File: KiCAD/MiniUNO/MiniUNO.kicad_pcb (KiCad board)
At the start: 2 copper layers, 22 x 18 mm, 19 parts, among them J1 USB_B_Micro, J2 Conn_01x11, J3 Conn_01x11, J4 Conn_01x07, U1 ATmega32U4-A, Y1 830108288709

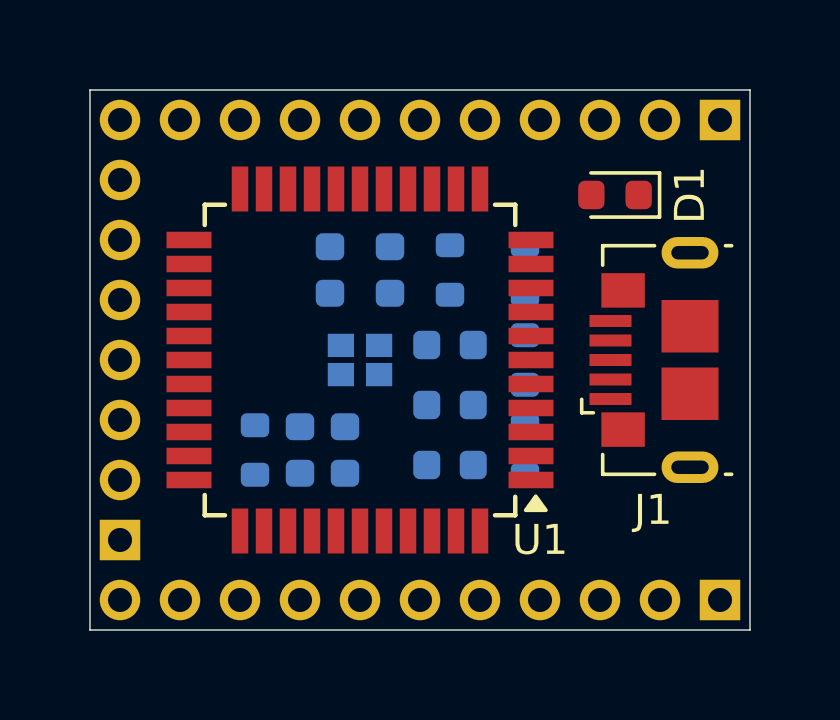
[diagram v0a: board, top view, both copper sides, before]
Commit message: Added a user controlled LED
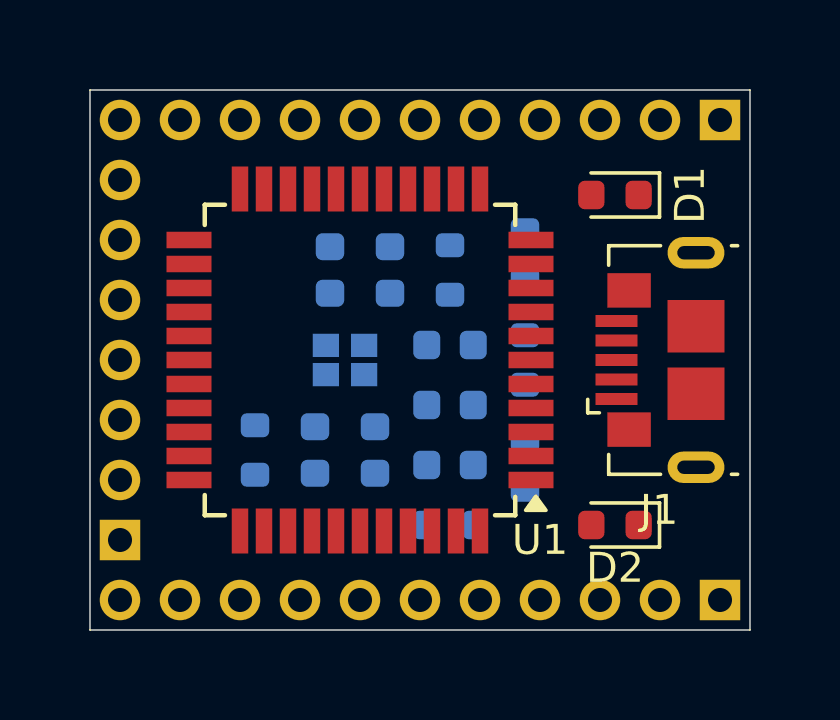
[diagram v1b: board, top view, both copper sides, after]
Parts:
- added D2: LED, LED_SMD:LED_0603_1608Metric, F.Cu at (8.50, 5.50)
- added R6: 330, Resistor_SMD:R_0603_1608Metric, B.Cu at (3.00, 5.50)
- moved C3 1.00 mm to (0.50, 3.00)
- moved C4 0.50 mm to (-1.50, 3.00)
- moved R2 0.50 mm to (5.50, 3.50)
- moved R5 0.50 mm to (5.50, -3.50)
- moved Y1 0.50 mm to (-0.50, 0.00)
- moved J1 0.20 mm to (10.0, 0.00)
- turned R3 to 90 degrees
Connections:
- C3 pad 1: VCC -> RESET
- C4 pad 1: VCC -> RESET
- C5 pad 1: VCC -> RESET
- J1 pad 1: VCC -> RESET
- J2 pad 1: unconnected-(J2-Pin_1-Pad1) -> RESET
- J2 pad 2: unconnected-(J2-Pin_2-Pad2) -> RESET
- J3 pad 1: unconnected-(J3-Pin_1-Pad1) -> GND
- R4 pad 2: VCC -> RESET
- R5 pad 1: VCC -> RESET
- U1 pad 1: unconnected-(U1-PE6-Pad1) -> USER_LED
- U1 pad 14: VCC -> RESET
- U1 pad 2: VCC -> RESET
- U1 pad 24: VCC -> RESET
- U1 pad 34: VCC -> RESET
- U1 pad 44: VCC -> RESET
- U1 pad 7: VCC -> RESET

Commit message: Minor changes
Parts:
- Y1: footprint Crystal:830108288709 -> Crystal:830108288709_Handsolderable
- moved R6 4.30 mm to (6.50, 3.00)
- moved R2 2.69 mm to (6.50, 1.00), turned to 180 degrees
- moved R1 1.41 mm to (6.50, -1.00), turned to 180 degrees
- moved R5 1.12 mm to (6.50, -3.00), turned to 0 degrees
- moved C1 0.50 mm to (-1.50, -3.00), turned to 90 degrees
- moved C2 0.50 mm to (0.50, -3.00)
- moved R4 0.50 mm to (2.50, -3.00)
- turned C7 to 180 degrees
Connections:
- C3 pad 1: RESET -> VCC
- C4 pad 1: RESET -> VCC
- C5 pad 1: RESET -> VCC
- C7 pad 1: Net-(U1-AREF) -> AREF
- J1 pad 1: RESET -> VCC
- J2 pad 1: RESET -> VCC
- J2 pad 10: unconnected-(J2-Pin_10-Pad10) -> D2/SDA
- J2 pad 11: unconnected-(J2-Pin_11-Pad11) -> D3/SCL
- J2 pad 3: unconnected-(J2-Pin_3-Pad3) -> SS
- J2 pad 4: unconnected-(J2-Pin_4-Pad4) -> SCK
- J2 pad 5: unconnected-(J2-Pin_5-Pad5) -> MOSI
- J2 pad 6: unconnected-(J2-Pin_6-Pad6) -> MISO
- J2 pad 7: unconnected-(J2-Pin_7-Pad7) -> CTS
- J2 pad 8: unconnected-(J2-Pin_8-Pad8) -> D0/RX
- J2 pad 9: unconnected-(J2-Pin_9-Pad9) -> D1/TX
- J3 pad 10: unconnected-(J3-Pin_10-Pad10) -> D12
- J3 pad 11: unconnected-(J3-Pin_11-Pad11) -> D11
- J3 pad 2: unconnected-(J3-Pin_2-Pad2) -> AREF
- J3 pad 3: unconnected-(J3-Pin_3-Pad3) -> A5
- J3 pad 4: unconnected-(J3-Pin_4-Pad4) -> A4
- J3 pad 5: unconnected-(J3-Pin_5-Pad5) -> A3
- J3 pad 6: unconnected-(J3-Pin_6-Pad6) -> A2
- J3 pad 7: unconnected-(J3-Pin_7-Pad7) -> A1
- J3 pad 8: unconnected-(J3-Pin_8-Pad8) -> A0
- J3 pad 9: unconnected-(J3-Pin_9-Pad9) -> D13/USER_LED
- J4 pad 1: unconnected-(J4-Pin_1-Pad1) -> D4
- J4 pad 2: unconnected-(J4-Pin_2-Pad2) -> D5
- J4 pad 3: unconnected-(J4-Pin_3-Pad3) -> D6
- J4 pad 4: unconnected-(J4-Pin_4-Pad4) -> D7
- J4 pad 5: unconnected-(J4-Pin_5-Pad5) -> D8
- J4 pad 6: unconnected-(J4-Pin_6-Pad6) -> D9
- J4 pad 7: unconnected-(J4-Pin_7-Pad7) -> D10
- R4 pad 1: Net-(U1-~{RESET}) -> RESET
- R4 pad 2: RESET -> VCC
- R5 pad 1: RESET -> VCC
- R6 pad 1: USER_LED -> D13/USER_LED
- U1 pad 1: USER_LED -> D7
- U1 pad 10: unconnected-(U1-PB2-Pad10) -> MOSI
- U1 pad 11: unconnected-(U1-PB3-Pad11) -> MISO
- U1 pad 12: unconnected-(U1-PB7-Pad12) -> D11
- U1 pad 13: Net-(U1-~{RESET}) -> RESET
- U1 pad 14: RESET -> VCC
- U1 pad 18: unconnected-(U1-PD0-Pad18) -> D3/SCL
- U1 pad 19: unconnected-(U1-PD1-Pad19) -> D2/SDA
- U1 pad 2: RESET -> VCC
- U1 pad 20: unconnected-(U1-PD2-Pad20) -> D0/RX
- U1 pad 21: unconnected-(U1-PD3-Pad21) -> D1/TX
- U1 pad 22: unconnected-(U1-PD5-Pad22) -> CTS
- U1 pad 24: RESET -> VCC
- U1 pad 25: unconnected-(U1-PD4-Pad25) -> D4
- U1 pad 26: unconnected-(U1-PD6-Pad26) -> D12
- U1 pad 27: unconnected-(U1-PD7-Pad27) -> D6
- U1 pad 28: unconnected-(U1-PB4-Pad28) -> D8
- U1 pad 29: unconnected-(U1-PB5-Pad29) -> D9
- U1 pad 30: unconnected-(U1-PB6-Pad30) -> D10
- U1 pad 31: unconnected-(U1-PC6-Pad31) -> D5
- U1 pad 32: unconnected-(U1-PC7-Pad32) -> D13/USER_LED
- U1 pad 34: RESET -> VCC
- U1 pad 36: unconnected-(U1-PF7-Pad36) -> A0
- U1 pad 37: unconnected-(U1-PF6-Pad37) -> A1
- U1 pad 38: unconnected-(U1-PF5-Pad38) -> A2
- U1 pad 39: unconnected-(U1-PF4-Pad39) -> A3
- U1 pad 40: unconnected-(U1-PF1-Pad40) -> A4
- U1 pad 41: unconnected-(U1-PF0-Pad41) -> A5
- U1 pad 42: Net-(U1-AREF) -> AREF
- U1 pad 44: RESET -> VCC
- U1 pad 7: RESET -> VCC
- U1 pad 8: unconnected-(U1-PB0-Pad8) -> SS
- U1 pad 9: unconnected-(U1-PB1-Pad9) -> SCK

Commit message: Lots more work
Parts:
- added C8: 1uF, Capacitor_SMD:C_0603_1608Metric, B.Cu at (11.8, -5.50)
- added C9: 1uF, Capacitor_SMD:C_0603_1608Metric, B.Cu at (11.8, 5.50)
- added IC1: AZ1117CR2-5.0TRG1, AZ1117CR2-5.0TRG1:AP738133Y13, B.Cu at (8.64, 0.00)
- added Q1: FDN340P, Package_TO_SOT_SMD:SuperSOT-3, B.Cu at (8.50, 4.75)
- added Q2: PMV48XP, Package_TO_SOT_SMD:SOT-23, B.Cu at (8.56, -4.75)
- moved J4 12.0 mm to (-8.00, -6.00), turned to 180 degrees
- moved C3 8.14 mm to (-5.00, -3.00)
- moved C5 1.58 mm to (1.50, 3.00)
- moved C6 1.58 mm to (1.50, -1.00)
- moved C7 1.58 mm to (1.50, 1.00)
- moved C1 1.50 mm to (-3.00, -3.00)
- moved C2 1.50 mm to (-1.00, -3.00)
- moved R1 1.50 mm to (5.00, -1.00)
- moved R2 1.50 mm to (5.00, 1.00)
- moved R5 1.50 mm to (5.00, -3.00)
- moved R6 1.50 mm to (5.00, 3.00)
- moved Y1 1.50 mm to (-2.00, 0.00)
- moved R4 1.00 mm to (1.50, -3.00), turned to 0 degrees
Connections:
- net Net-(U1-D+) renamed D+
- net Net-(U1-D-) renamed D-
- net Net-(U1-UCAP) renamed UCAP
- C3 pad 1: VCC -> +5V
- C4 pad 1: VCC -> +5V
- C5 pad 1: VCC -> +5V
- J1 pad 1: VCC -> VUSB
- J2 pad 1: VCC -> +5V
- J3 pad 2: AREF -> VIN
- R4 pad 2: VCC -> +5V
- R5 pad 1: VCC -> +5V
- U1 pad 14: VCC -> +5V
- U1 pad 2: VCC -> +5V
- U1 pad 24: VCC -> +5V
- U1 pad 34: VCC -> +5V
- U1 pad 44: VCC -> +5V
- U1 pad 7: VCC -> VUSB
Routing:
- net +5V: track 0.00 -> 89.8 mm, vias 0 -> 4
- net GND: track 0.00 -> 88.0 mm, vias 0 -> 5
- net Net-(J1-D-): track 0.00 -> 27.4 mm, vias 0 -> 3
- net D11: track 0.00 -> 20.6 mm, vias 0 -> 1
- net VIN: track 0.00 -> 18.5 mm
- net D13/USER_LED: track 0.00 -> 17.2 mm
- net Net-(IC1-IN): track 0.00 -> 16.3 mm
- net D7: track 0.00 -> 16.2 mm, vias 0 -> 3
- net A4: track 0.00 -> 16.0 mm, vias 0 -> 1
- net RESET: track 0.00 -> 13.5 mm, vias 0 -> 2
- net D+: track 0.00 -> 12.3 mm, vias 0 -> 1
- net D12: track 0.00 -> 11.8 mm, vias 0 -> 2
- net D3/SCL: track 0.00 -> 9.88 mm
- net VUSB: track 0.00 -> 8.99 mm, vias 0 -> 1
- net D5: track 0.00 -> 8.89 mm, vias 0 -> 1
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- added copper zone on B.Cu, net GND
- added copper zone on F.Cu, net GND
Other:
- board text added: "5V"
- board text added: "GND"
- board text added: "PWR"
- board text added: "RST"
- board text added: "VIN"

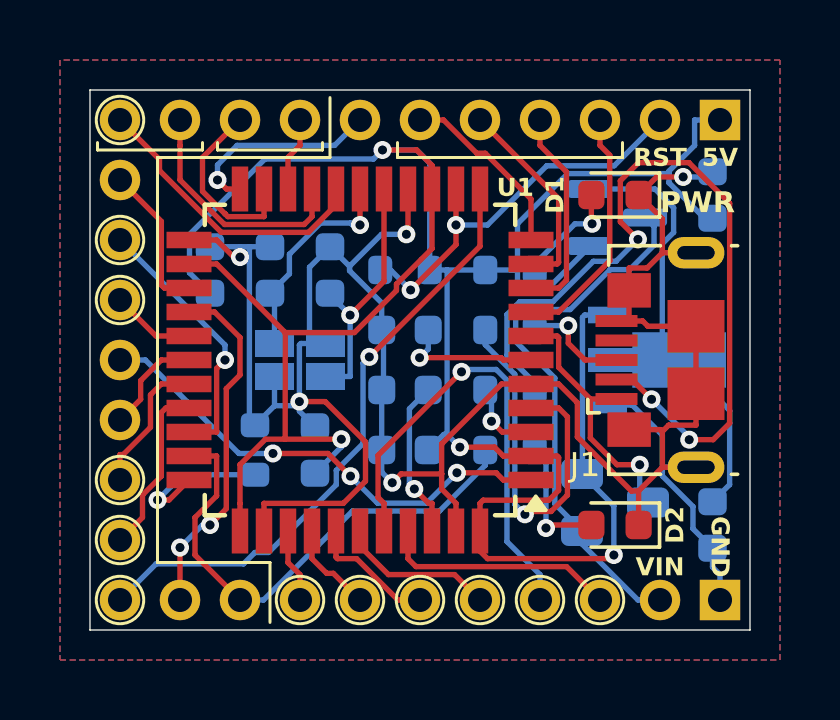
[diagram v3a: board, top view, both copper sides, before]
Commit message: Addec pulldown resistors to the VUSB and VIN MOSFETS. Made the adapter PCB
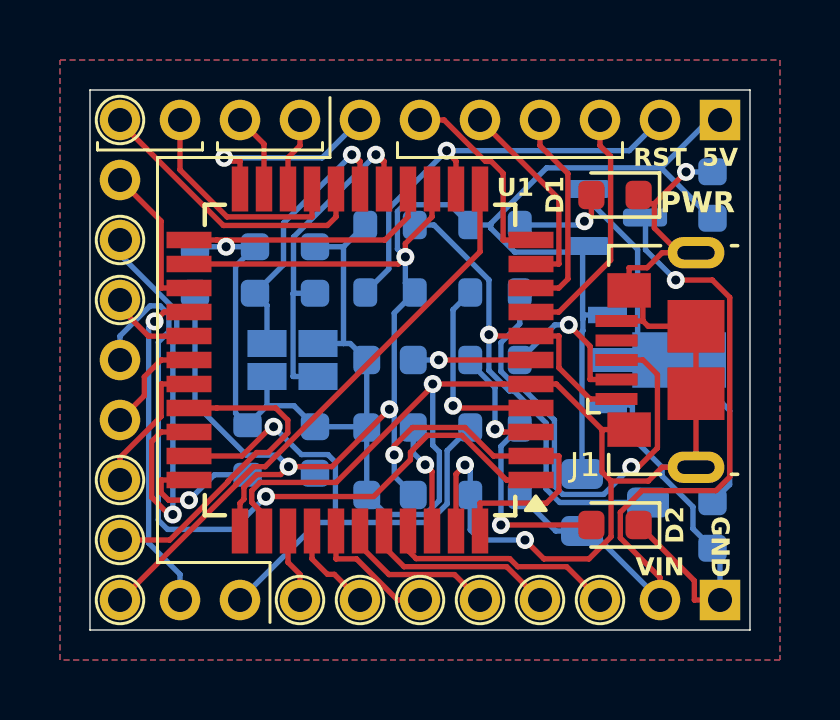
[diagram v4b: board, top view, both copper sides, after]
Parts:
- added R7: 10k, Resistor_SMD:R_0603_1608Metric, B.Cu at (1.00, -4.50)
- added R8: 10k, Resistor_SMD:R_0603_1608Metric, B.Cu at (4.50, 4.50)
- C8: value 1uF -> 22uF
- C9: value 1uF -> 10uF
- moved C5 1.58 mm to (1.00, 4.50)
- moved R5 1.58 mm to (4.50, -4.50)
- moved C7 1.35 mm to (1.00, 2.25)
- moved R1 1.35 mm to (4.50, -2.25)
- moved C6 1.12 mm to (1.00, 0.00)
- moved R2 1.12 mm to (4.50, 0.00)
- moved R4 0.90 mm to (1.00, -2.25)
- moved R6 0.90 mm to (4.50, 2.25)
- moved C1 0.50 mm to (-3.50, -3.00)
- moved C2 0.50 mm to (-1.50, -3.00)
- moved C3 0.50 mm to (-5.50, -3.00)
- moved R3 0.25 mm to (-3.75, 3.00)
- moved Y1 0.25 mm to (-2.25, 0.00)
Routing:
- net Net-(J1-D-): track 27.4 -> 5.11 mm, vias 3 -> 1
- net GND: track 88.0 -> 105.0 mm
- net +5V: track 89.8 -> 74.8 mm
- net Net-(J1-D+): track 3.61 -> 15.8 mm
- net VUSB: track 8.99 -> 20.4 mm
- net A4: track 16.0 -> 6.46 mm, vias 1 -> 0
- net D7: track 16.2 -> 24.6 mm, vias 3 -> 1
- net VIN: track 18.5 -> 24.3 mm, vias 0 -> 1
- net D+: track 12.3 -> 6.64 mm
- net D5: track 8.89 -> 14.2 mm
- net D10: track 5.80 -> 11.0 mm
- net D1/TX: track 6.22 -> 2.63 mm
- net XTAL2: track 8.55 -> 11.4 mm
- net Net-(D2-A): track 4.31 -> 6.52 mm
- net Net-(IC1-IN): track 16.3 -> 14.3 mm
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
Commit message: Finalized design v1
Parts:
- moved C6 4.30 mm to (4.50, 2.50)
- moved R5 3.54 mm to (1.00, -5.00)
- moved R7 3.54 mm to (4.50, -5.00)
- moved R6 3.51 mm to (1.00, 2.50)
- moved R2 3.50 mm to (1.00, 0.00)
- moved C5 2.92 mm to (-1.50, 3.00), turned to 90 degrees
- moved C7 2.75 mm to (1.00, 5.00)
- moved C4 2.00 mm to (-3.50, 3.00)
- moved R3 1.75 mm to (-5.50, 3.00)
- moved Y1 1.25 mm to (-3.50, 0.00)
- moved R8 0.50 mm to (4.50, 5.00)
- moved R1 0.25 mm to (4.50, -2.50)
- moved R4 0.25 mm to (1.00, -2.50)
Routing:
- net Net-(J1-D-): track 5.11 -> 17.6 mm
- net Net-(D2-A): track 6.52 -> 13.9 mm, vias 1 -> 3
- net D7: track 24.6 -> 17.8 mm
- net RESET: track 14.8 -> 21.3 mm, vias 1 -> 2
- net Net-(J1-D+): track 15.8 -> 10.7 mm
- net D10: track 11.0 -> 5.90 mm
- net Net-(IC1-IN): track 14.3 -> 18.8 mm
- net D13/USER_LED: track 18.9 -> 14.5 mm
- net D11: track 18.9 -> 22.8 mm, vias 0 -> 3
- net +5V: track 74.8 -> 78.7 mm, vias 4 -> 5
- net A4: track 6.46 -> 10.2 mm, vias 0 -> 1
- net D5: track 14.2 -> 10.6 mm
- net Net-(D1-A): track 3.18 -> 6.69 mm
- net D-: track 3.89 -> 7.20 mm
- net XTAL2: track 11.4 -> 8.17 mm
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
